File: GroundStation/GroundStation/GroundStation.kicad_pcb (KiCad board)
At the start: 2 copper layers, 70 parts, among them J1 SD_Card_Receptacle, J4 Conn_Coaxial, J5 Conn_01x02, P1 USB_C_Plug_USB2.0, Q1 TSM3481CX6 RFG, U1 STM32F103C8Tx, U101 LD1117S33TR_SOT223, U2 E22-400T30S_LoRa, U4 TPS54538RQFR, U9 NEO-M9N-00B

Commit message: second need freerouting
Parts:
- removed AE1, AE2: Antenna, Connector_Coaxial:SMA_Molex_73251-1153_EdgeMount_Horizontal
- removed C3, C4, C5: 0.1uF, Capacitor_SMD:C_0805_2012Metric_Pad1.18x1.45mm_HandSolder
- removed E80-900M2213S101: ~, RF:E80-900M2213S
- removed R3_up2: 10k, Resistor_SMD:R_0805_2012Metric_Pad1.20x1.40mm_HandSolder
- removed U2: E22-400T30S_LoRa, Library:e22-400t30s_Package
- added C43: 100n, Capacitor_SMD:C_0805_2012Metric_Pad1.18x1.45mm_HandSolder, F.Cu at (133.9, 61.0)
- added C44: 100u, Capacitor_SMD:C_0805_2012Metric_Pad1.18x1.45mm_HandSolder, F.Cu at (133.9, 64.0)
- added C45: 100n, Capacitor_SMD:C_0805_2012Metric_Pad1.18x1.45mm_HandSolder, F.Cu at (176.5, 43.0)
- added C46: 22u, Capacitor_SMD:C_0805_2012Metric_Pad1.18x1.45mm_HandSolder, F.Cu at (176.5, 46.0)
- added R30: 22ohm, Resistor_SMD:R_0805_2012Metric_Pad1.20x1.40mm_HandSolder, F.Cu at (118.8, 61.1)
- added R31: 22ohm, Resistor_SMD:R_0805_2012Metric_Pad1.20x1.40mm_HandSolder, F.Cu at (118.8, 64.1)
- added R32: 10k, Resistor_SMD:R_0805_2012Metric_Pad1.20x1.40mm_HandSolder, F.Cu at (124.8, 61.1)
- added R33: 10k, Resistor_SMD:R_0805_2012Metric_Pad1.20x1.40mm_HandSolder, F.Cu at (181.5, 43.0)
- added U10: E22-400T30S, Library:e22-400t30s_Package, F.Cu at (115.7, 15.3)
- added U11: E80-900M23313S, RF:E80-900M2213S, F.Cu at (181.5, 28.0)
- P1: footprint Connector_USB:USB3_A_Molex_48393-001 -> Connector_USB:USB_C_Receptacle_JAE_DX07S016JA1R1500
- moved R16(PG_pull_up)101 75.9 mm to (152.3, 24.2)
- moved R2 64.7 mm to (165.4, 83.2)
- moved C39 49.8 mm to (177.8, 54.6), turned to 0 degrees
- moved C40 49.5 mm to (177.8, 57.6), turned to 0 degrees
- moved R16 43.9 mm to (118.9, 81.6)
- moved C16 43.6 mm to (133.8, 68.5)
- moved J4 38.0 mm to (177.1, 98.6)
- moved R27 37.6 mm to (187.8, 54.6), turned to 0 degrees
- moved Q1 36.4 mm to (131.4, 105.3), turned to 0 degrees
- moved P1 34.1 mm to (180.5, 118.6)
- moved R26 33.2 mm to (187.8, 64.6), turned to 0 degrees
- moved C2 32.8 mm to (157.6, 88.8)
- moved J1 32.3 mm to (155.0, 105.0)
- moved R2_up1 32.0 mm to (151.5, 88.7)
- moved R18 32.0 mm to (131.4, 120.1)
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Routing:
- net GND: track 551.6 -> 0.00 mm, vias 8 -> 0
- net 3.3V: track 210.8 -> 0.00 mm, vias 2 -> 0
- net BUCK_5V: track 168.7 -> 0.00 mm, vias 4 -> 0
- net V_BAT+: track 159.7 -> 0.00 mm, vias 2 -> 0
- net +3.3V: track 119.1 -> 0.00 mm
- net Net-(U9-SAFEBOOT_N): track 77.5 -> 0.00 mm
- net Net-(J4-In): track 59.8 -> 0.00 mm
- net USART1_GPS_RESET: track 53.8 -> 0.00 mm, vias 2 -> 0
- net USART2_LoRa1_NRST: track 47.1 -> 0.00 mm
- net Net-(U1-VDDA): track 44.1 -> 0.00 mm, vias 3 -> 0
- net Net-(D102-A1): track 32.7 -> 0.00 mm, vias 2 -> 0
- net Net-(C41-Pad1): track 30.2 -> 0.00 mm, vias 2 -> 0
- net SPI2_SDcard_CS: track 28.4 -> 0.00 mm
- net USART1_GPS_TX: track 26.2 -> 0.00 mm, vias 2 -> 0
- net SPI2_SDcard_SCK: track 25.7 -> 0.00 mm
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
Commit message: jpush
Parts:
- moved C43 55.2 mm to (89.0, 93.0)
- moved R17 48.1 mm to (113.9, 59.5)
- moved 3V3 48.1 mm to (113.5, 52.5)
- moved Buck_5v101 48.1 mm to (118.5, 52.5)
- moved GND101 48.1 mm to (123.5, 52.5)
- moved D101 48.1 mm to (119.5, 63.7)
- moved D2 48.1 mm to (114.0, 63.8)
- moved R16(PG_pull_up)101 48.1 mm to (119.5, 59.3)
- moved V_BAT+101 48.1 mm to (128.3, 52.5)
- moved TP1 48.1 mm to (133.5, 52.7)
- moved R15 47.5 mm to (83.8, 109.9)
- moved C12 47.5 mm to (91.3, 108.4)
- moved C13 47.5 mm to (91.3, 111.4)
- moved F1 47.5 mm to (91.0, 151.8)
- moved C10 47.5 mm to (109.8, 104.8)
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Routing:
- net GND: track 0.00 -> 692.8 mm, vias 0 -> 5
- net +3.3V: track 0.00 -> 297.1 mm, vias 0 -> 4
- net 3.3V: track 0.00 -> 158.8 mm, vias 0 -> 6
- net V_BAT+: track 0.00 -> 132.7 mm, vias 0 -> 6
- net BUCK_5V: track 0.00 -> 118.0 mm, vias 0 -> 3
- net USART2_LoRa1_AUX: track 0.00 -> 84.3 mm, vias 0 -> 2
- net USART2_LoRa1_M1: track 0.00 -> 82.4 mm, vias 0 -> 4
- net SPI1_LoRa2_MISO: track 0.00 -> 78.0 mm, vias 0 -> 2
- net USART2_LoRa1_M0: track 0.00 -> 76.3 mm, vias 0 -> 2
- net USB_5V: track 0.00 -> 71.1 mm, vias 0 -> 2
- net SPI1_LoRa2_SCK: track 0.00 -> 70.3 mm, vias 0 -> 2
- net SPI1_LoRa2_MOSI: track 0.00 -> 70.1 mm, vias 0 -> 4
- net Net-(D101-A): track 0.00 -> 70.1 mm, vias 0 -> 4
- net SPI1_LoRa2_CS: track 0.00 -> 67.6 mm, vias 0 -> 2
- net USART2_LoRa1_NRST: track 0.00 -> 64.7 mm
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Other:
- board outline added: 104 x 127.5 mm

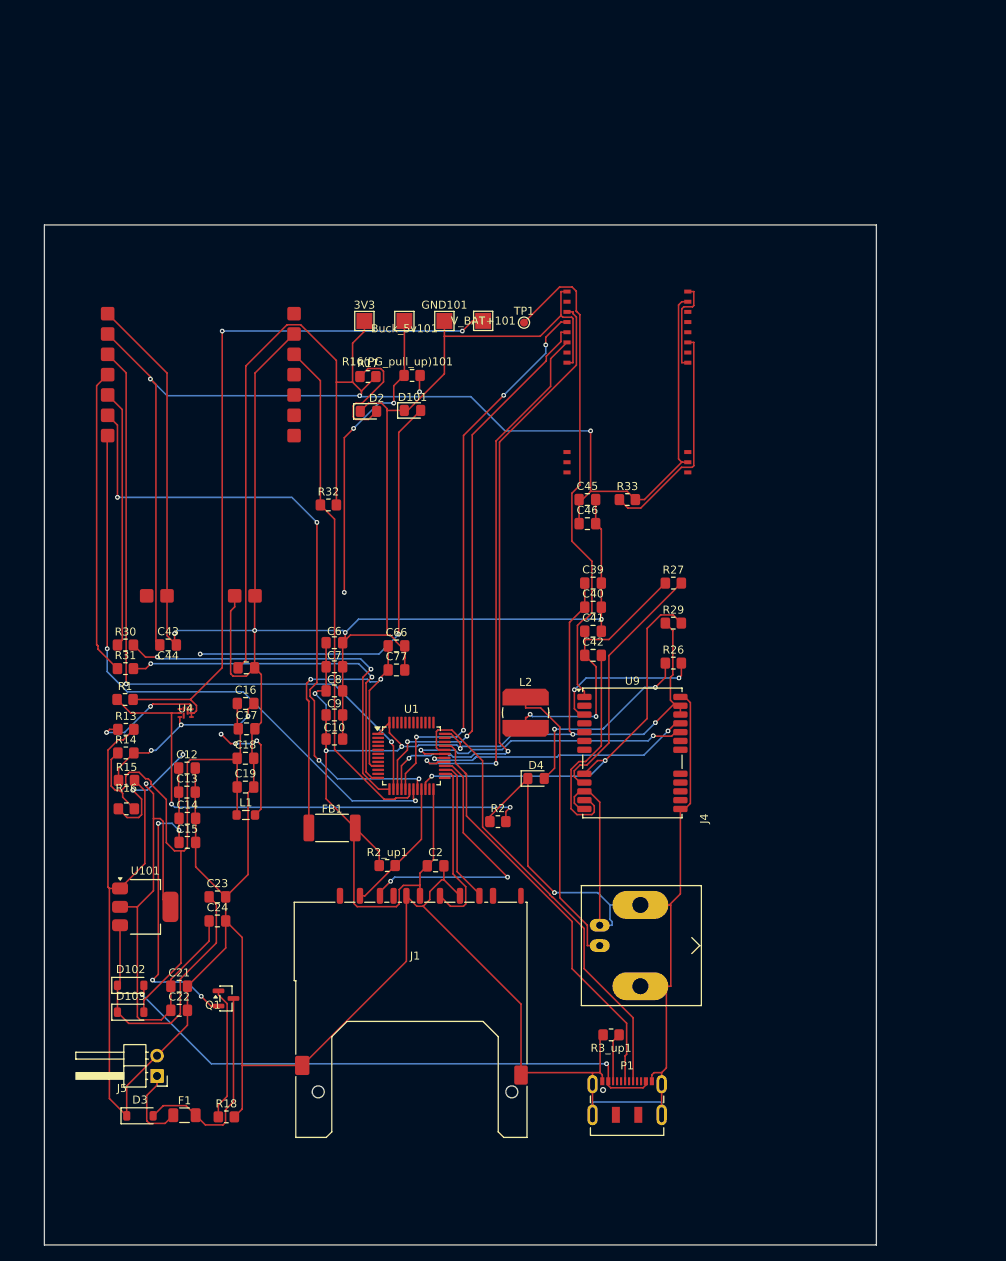
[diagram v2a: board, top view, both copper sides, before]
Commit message: Ray say: GroundStation finish PCB lay out
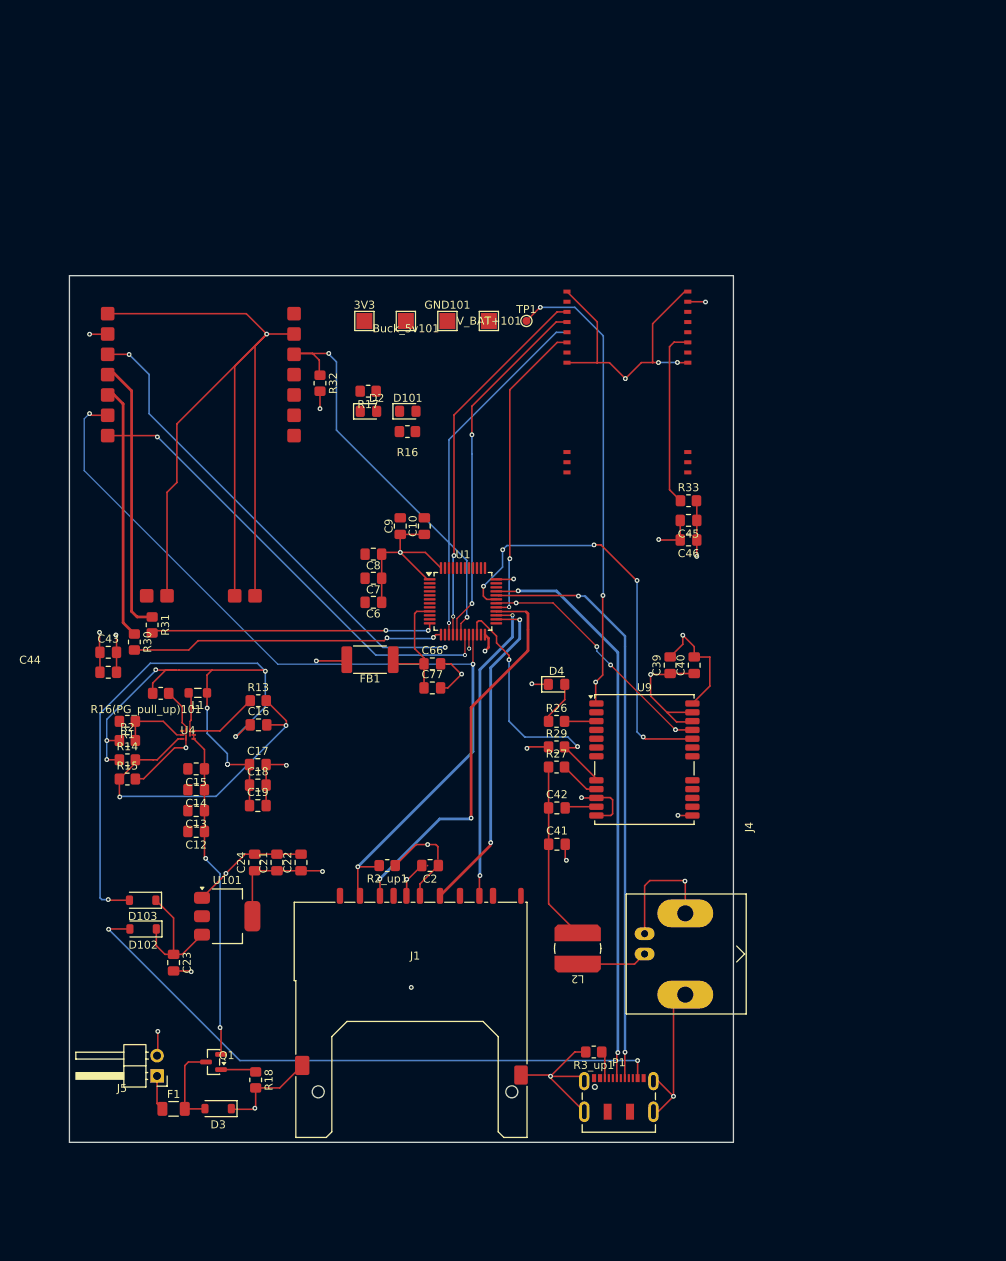
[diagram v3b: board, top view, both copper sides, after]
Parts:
- moved R16 58.8 mm to (118.9, 66.3), turned to 180 degrees
- moved R16(PG_pull_up)101 50.7 mm to (88.0, 99.0)
- moved R2 47.4 mm to (83.9, 104.9)
- moved L2 30.2 mm to (140.2, 130.9), turned to 180 degrees
- moved C10 28.9 mm to (121.0, 78.1), turned to 90 degrees
- moved R27 27.2 mm to (137.5, 108.3)
- moved C41 27.0 mm to (137.6, 117.9)
- moved C9 25.0 mm to (118.0, 78.1), turned to 90 degrees
- moved C22 23.9 mm to (105.6, 120.2), turned to 90 degrees
- moved FB1 21.6 mm to (114.2, 94.8), turned to 180 degrees
- moved R29 21.3 mm to (137.5, 105.7)
- moved U1 20.4 mm to (125.8, 87.5)
- moved C21 19.7 mm to (102.6, 120.2), turned to 90 degrees
- moved C42 19.6 mm to (137.6, 113.4)
- moved C8 17.8 mm to (114.6, 81.7), turned to 180 degrees
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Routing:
- net GND: track 692.8 -> 329.1 mm, vias 5 -> 23
- net +3.3V: track 297.1 -> 33.2 mm, vias 4 -> 6
- net 3.3V: track 158.8 -> 66.8 mm, vias 6 -> 7
- net V_BAT+: track 132.7 -> 41.6 mm, vias 6 -> 2
- net SPI2_SDcard_CS: track 16.9 -> 107.5 mm, vias 0 -> 3
- net USART2_LoRa1_M1: track 82.4 -> 3.93 mm, vias 4 -> 1
- net Net-(D101-A): track 70.1 -> 0.00 mm, vias 4 -> 0
- net Net-(U4-EN): track 64.4 -> 8.95 mm, vias 2 -> 0
- net SPI1_LoRa2_MISO: track 78.0 -> 46.9 mm
- net Net-(U1-VDDA): track 45.1 -> 15.8 mm, vias 2 -> 0
- net SPI1_LoRa2_CS: track 67.6 -> 38.5 mm
- net Net-(J4-In): track 36.9 -> 8.89 mm
- net Net-(U9-VCC_RF): track 31.8 -> 5.12 mm
- net SPI1_LoRa2_SCK: track 70.3 -> 44.5 mm, vias 2 -> 1
- net SPI1_LoRa2_MOSI: track 70.1 -> 45.4 mm, vias 4 -> 2
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- added copper zone on In2.Cu, net +3.3V
- added copper zone on In1.Cu, net GND
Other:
- board size 104 x 127.5 mm -> 83 x 108.3 mm
- copper layers 2 -> 4
